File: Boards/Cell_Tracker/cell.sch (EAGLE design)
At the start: 26 parts, among them U2 LMR16020

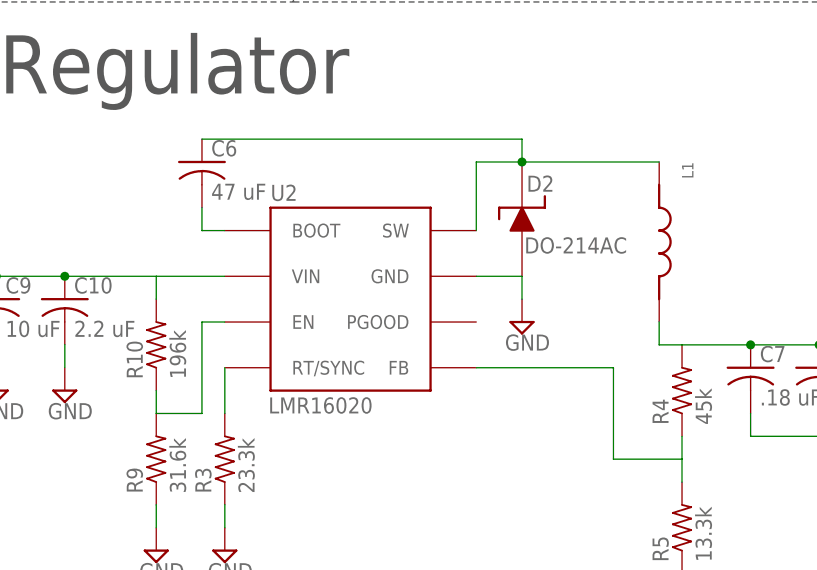
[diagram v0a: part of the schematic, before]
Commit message: Updated the inductor and mosfet in cell schematic
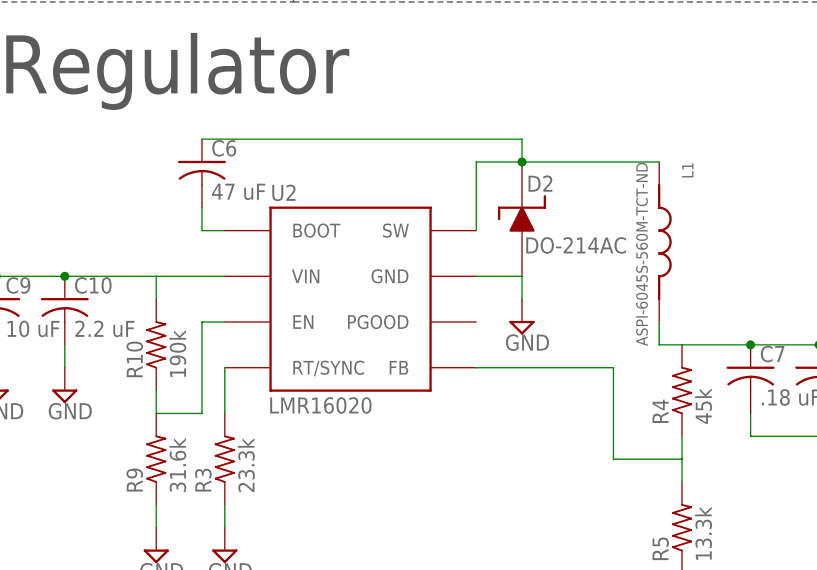
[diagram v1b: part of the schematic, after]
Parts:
- L1: value (none) -> ASPI-6045S-560M-TCT-ND; device inductors:587-2099-1-ND -> inductors:ASPI-6045S-560M-TCT-ND
- R10: value 196k -> 190k
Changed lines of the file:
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@@
 <?xml version="1.0" encoding="utf-8"?>
 <!DOCTYPE eagle SYSTEM "eagle.dtd">
-<eagle version="9.3.0">
+<eagle version="7.6.0">
 <drawing>
 <settings>
 <setting alwaysvectorfont="no"/>
-<setting keepoldvectorfont="yes"/>
 <setting verticaltext="up"/>
 </settings>
@@
 <part name="JP3" library="pinhead" deviceset="PINHD-1X2" device=""/>
 <part name="R9" library="resistor" deviceset="R-US_" device="R0603" value="31.6k"/>
-<part name="R10" library="resistor" deviceset="R-US_" device="R0603" value="196k"/>
+<part name="R10" library="resistor" deviceset="R-US_" device="R0603" value="190k"/>
 <part name="SUPPLY1" library="supply2" deviceset="GND" device=""/>
-<part name="L1" library="inductors" deviceset="587-2099-1-ND" device=""/>
+<part name="L1" library="inductors" deviceset="ASPI-6045S-560M-TCT-ND" device=""/>
 <part name="+3V6" library="supply1" deviceset="+3V3" device=""/>
 <part name="SUPPLY2" library="supply2" deviceset="GND" device=""/>

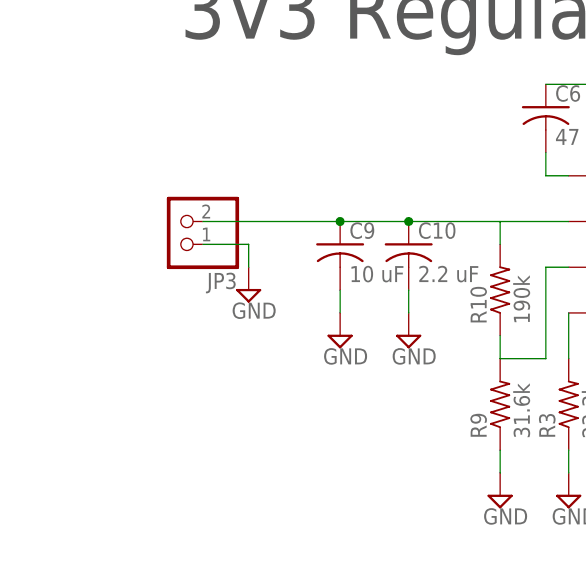
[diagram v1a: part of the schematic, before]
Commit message: put connector on cell board, plus lots of cad work
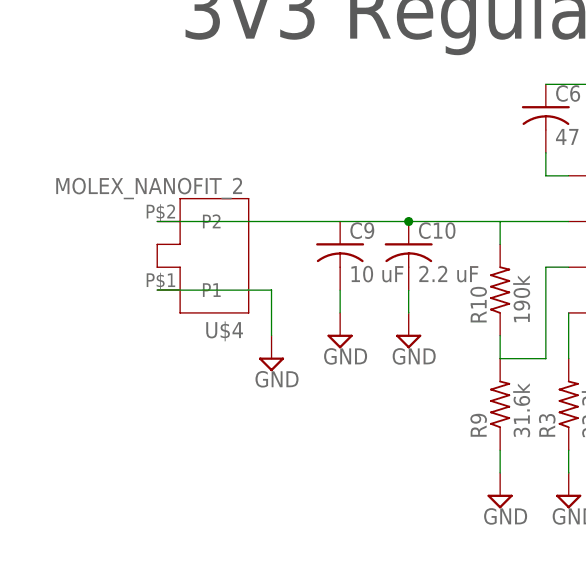
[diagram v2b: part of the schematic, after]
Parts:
- removed JP3: (no value), pinhead:PINHD-1X2
- added U$4: MOLEX_NANOFIT_2, cmdLibs:MOLEX_NANOFIT_2
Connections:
- net GND: now also U$4.P1; no longer JP3.1
- net VIN: now also U$4.P2; no longer JP3.2
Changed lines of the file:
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@@
 <part name="U2" library="HASP" deviceset="LMR16020" device=""/>
 <part name="D2" library="HASP" deviceset="DO-214AC" device=""/>
-<part name="JP3" library="pinhead" deviceset="PINHD-1X2" device=""/>
 <part name="R9" library="resistor" deviceset="R-US_" device="R0603" value="31.6k"/>
 <part name="R10" library="resistor" deviceset="R-US_" device="R0603" value="190k"/>
@@
 <part name="+3V7" library="supply1" deviceset="+3V3" device=""/>
 <part name="U$2" library="cmdLibs" deviceset="SI1013" device=""/>
+<part name="U$4" library="cmdLibs" deviceset="MOLEX_NANOFIT_2" device=""/>
 </parts>
 <sheets>
@@
 <attribute name="VALUE" x="86.614" y="91.44" size="1.778" layer="95"/>
 </instance>
-<instance part="JP3" gate="G$1" x="10.16" y="88.9" smashed="yes" rot="R180">
-<attribute name="NAME" x="16.51" y="83.185" size="1.778" layer="95" rot="R180"/>
-<attribute name="VALUE" x="16.51" y="93.98" size="1.778" layer="96" rot="R180"/>
-</instance>
 <instance part="R9" gate="G$1" x="45.72" y="68.58" smashed="yes" rot="R90">
 <attribute name="NAME" x="44.2214" y="64.77" size="1.778" layer="95" rot="R90"/>
@@
 <attribute name="VALUE" x="127" y="78.74" size="1.778" layer="96"/>
 </instance>
-<instance part="SUPPLY2" gate="GND" x="17.78" y="81.28" smashed="yes">
-<attribute name="VALUE" x="15.875" y="78.105" size="1.778" layer="96"/>
+<instance part="SUPPLY2" gate="GND" x="20.32" y="73.66" smashed="yes">
+<attribute name="VALUE" x="18.415" y="70.485" size="1.778" layer="96"/>
 </instance>
 <instance part="U$3" gate="G$1" x="208.28" y="172.72" smashed="yes"/>
@@
 <attribute name="NAME" x="209.042" y="132.08" size="1.778" layer="95" rot="R180"/>
 </instance>
+<instance part="U$4" gate="G$1" x="10.16" y="83.82" rot="R180"/>
 </instances>
 <busses>
@@
 </segment>
 <segment>
-<pinref part="JP3" gate="G$1" pin="1"/>
-<wire x1="12.7" y1="86.36" x2="17.78" y2="86.36" width="0.1524" layer="91"/>
-<wire x1="17.78" y1="86.36" x2="17.78" y2="83.82" width="0.1524" layer="91"/>
+<wire x1="20.32" y1="81.28" x2="20.32" y2="76.2" width="0.1524" layer="91"/>
 <pinref part="SUPPLY2" gate="GND" pin="GND"/>
+<pinref part="U$4" gate="G$1" pin="P1"/>
+<wire x1="7.62" y1="81.28" x2="20.32" y2="81.28" width="0.1524" layer="91"/>
 </segment>
 <segment>
@@
 <pinref part="C9" gate="G$1" pin="1"/>
 <pinref part="U2" gate="G$1" pin="VIN"/>
-<pinref part="JP3" gate="G$1" pin="2"/>
-<junction x="27.94" y="88.9"/>
-<wire x1="27.94" y1="88.9" x2="12.7" y2="88.9" width="0.1524" layer="91"/>
 <pinref part="R10" gate="G$1" pin="2"/>
 <wire x1="45.72" y1="86.36" x2="45.72" y2="88.9" width="0.1524" layer="91"/>
-</segment>
-</net>
+<pinref part="U$4" gate="G$1" pin="P2"/>
+<wire x1="7.62" y1="88.9" x2="27.94" y2="88.9" width="0.1524" layer="91"/>
+</segment>
+</net>

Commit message: All of the changes with CAD and electronics since switching to the microclasp connectors
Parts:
- added R7: (no value), resistor:R-US_R0603
- added U$5: (no value), NR_connectors:MICROCLASP
- U$4: value MOLEX_NANOFIT_2 -> (none); device cmdLibs:MOLEX_NANOFIT_2 -> NR_connectors:MICROCLASP
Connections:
- new net N$12: R7.1, U$5.P$1
- new net N$15: U$1.4/CAN-RX-PWM
- new net N$16: U$1.5/PWM
- new net N$33: U$1.6/PWM
- new net SWITCH_LED: R7.2, U$1.3/CAN-TX/PWM
- net GND: now also U$4.P$2, U$5.P$2; no longer U$4.P1
- net VIN: now also U$4.P$1; no longer U$4.P2
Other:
- note added: "LED Status"
- moved on the sheet: C10, C6, C7, C8, C9, COIN, D2, L1, R1, R10, R11, R2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

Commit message: fixes and design review slides
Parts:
- removed R7: (no value), resistor:R-US_R0603
- removed U$5: (no value), NR_connectors:MICROCLASP
- added R8: (no value), resistor:R-US_R0603
- R10: value 190k -> 195k
- R9: value 31.6k -> 39k
- U$4: value (none) -> MICROCLASP_4; device NR_connectors:MICROCLASP -> NR_connectors:MICROCLASP_4
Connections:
- removed net N$12: R7.1, U$5.P$1
- new net N$13: R8.2, U$4.P$2
- net GND: now also U$4.P$3, U$4.P$4; no longer U$4.P$2, U$5.P$2
- net SWITCH_LED: now also R8.1; no longer R7.2
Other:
- note removed: "LED Status"
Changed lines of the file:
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@@
 <part name="U2" library="HASP" deviceset="LMR16020" device=""/>
 <part name="D2" library="HASP" deviceset="DO-214AC" device=""/>
-<part name="R9" library="resistor" deviceset="R-US_" device="R0603" value="31.6k"/>
-<part name="R10" library="resistor" deviceset="R-US_" device="R0603" value="190k"/>
+<part name="R9" library="resistor" deviceset="R-US_" device="R0603" value="39k"/>
+<part name="R10" library="resistor" deviceset="R-US_" device="R0603" value="195k"/>
 <part name="SUPPLY1" library="supply1" deviceset="GND" device=""/>
 <part name="L1" library="inductors" deviceset="ASPI-6045S-560M-TCT-ND" device=""/>
 <part name="+3V6" library="supply1" deviceset="+3V3" device=""/>
-<part name="SUPPLY2" library="supply1" deviceset="GND" device=""/>
 <part name="U$3" library="NR_connectors" deviceset="MICRO_SD" device=""/>
 <part name="GND6" library="supply1" deviceset="GND" device=""/>
@@
 <part name="U$2" library="cmdLibs" deviceset="SI1013" device=""/>
 <part name="FRAME1" library="frames" deviceset="A4L-LOC" device=""/>
-<part name="U$4" library="NR_connectors" deviceset="MICROCLASP" device=""/>
-<part name="U$5" library="NR_connectors" deviceset="MICROCLASP" device=""/>
-<part name="GND1" library="supply1" deviceset="GND" device=""/>
-<part name="R7" library="resistor" deviceset="R-US_" device="R0603"/>
+<part name="U$4" library="NR_connectors" deviceset="MICROCLASP_4" device=""/>
+<part name="R8" library="resistor" deviceset="R-US_" device="R0603"/>
+<part name="SUPPLY2" library="supply1" deviceset="GND" device=""/>
 </parts>
 <sheets>
@@
 <wire x1="7.62" y1="88.9" x2="50.8" y2="88.9" width="0.1524" layer="97" style="longdash"/>
 <wire x1="50.8" y1="175.26" x2="50.8" y2="88.9" width="0.1524" layer="97" style="longdash"/>
-<text x="121.92" y="96.52" size="6.4516" layer="97">LED Status</text>
 <wire x1="144.78" y1="109.22" x2="144.78" y2="175.26" width="0.1524" layer="97" style="longdash"/>
 <wire x1="119.38" y1="88.9" x2="50.8" y2="88.9" width="0.1524" layer="97" style="longdash"/>
@@
 <wire x1="256.54" y1="109.22" x2="170.18" y2="109.22" width="0.1524" layer="97" style="longdash"/>
 <wire x1="170.18" y1="109.22" x2="144.78" y2="109.22" width="0.1524" layer="97" style="longdash"/>
-<wire x1="170.18" y1="109.22" x2="170.18" y2="71.12" width="0.1524" layer="97" style="longdash"/>
-<wire x1="170.18" y1="71.12" x2="119.38" y2="71.12" width="0.1524" layer="97" style="longdash"/>
 </plain>
 <instances>
@@
 <attribute name="VALUE" x="132.08" y="38.1" size="1.778" layer="96"/>
 </instance>
-<instance part="SUPPLY2" gate="1" x="25.4" y="33.02" smashed="yes">
-<attribute name="VALUE" x="23.495" y="29.845" size="1.778" layer="96"/>
-</instance>
 <instance part="U$3" gate="G$1" x="187.96" y="134.62" smashed="yes"/>
 <instance part="GND6" gate="1" x="208.28" y="124.46" smashed="yes">
@@
 </instance>
 <instance part="FRAME1" gate="G$1" x="0" y="0"/>
-<instance part="U$4" gate="G$1" x="10.16" y="48.26"/>
-<instance part="U$5" gate="G$1" x="127" y="86.36"/>
-<instance part="GND1" gate="1" x="139.7" y="78.74" smashed="yes">
-<attribute name="VALUE" x="137.16" y="76.2" size="1.778" layer="96"/>
-</instance>
-<instance part="R7" gate="G$1" x="144.78" y="86.36"/>
+<instance part="U$4" gate="G$1" x="7.62" y="43.18"/>
+<instance part="R8" gate="G$1" x="25.4" y="40.64" rot="R90"/>
+<instance part="SUPPLY2" gate="1" x="20.32" y="33.02" smashed="yes">
+<attribute name="VALUE" x="18.415" y="29.845" size="1.778" layer="96"/>
+</instance>
 </instances>
 <busses>
@@
 <wire x1="50.8" y1="22.86" x2="50.8" y2="20.32" width="0.1524" layer="91"/>
 <pinref part="SUPPLY1" gate="1" pin="GND"/>
-</segment>
-<segment>
-<pinref part="SUPPLY2" gate="1" pin="GND"/>
-<pinref part="U$4" gate="G$1" pin="P$2"/>
-<wire x1="25.4" y1="35.56" x2="25.4" y2="45.72" width="0.1524" layer="91"/>
-<wire x1="25.4" y1="45.72" x2="20.32" y2="45.72" width="0.1524" layer="91"/>
 </segment>
 <segment>
@@
 </segment>
 <segment>
-<pinref part="U$5" gate="G$1" pin="P$2"/>
-<wire x1="137.16" y1="83.82" x2="139.7" y2="83.82" width="0.1524" layer="91"/>
-<wire x1="139.7" y1="83.82" x2="139.7" y2="81.28" width="0.1524" layer="91"/>
-<pinref part="GND1" gate="1" pin="GND"/>
+<pinref part="U$4" gate="G$1" pin="P$3"/>
+<wire x1="17.78" y1="43.18" x2="20.32" y2="43.18" width="0.1524" layer="91"/>
+<wire x1="20.32" y1="43.18" x2="20.32" y2="40.64" width="0.1524" layer="91"/>
+<pinref part="U$4" gate="G$1" pin="P$4"/>
+<wire x1="20.32" y1="40.64" x2="20.32" y2="35.56" width="0.1524" layer="91"/>
+<wire x1="17.78" y1="40.64" x2="20.32" y2="40.64" width="0.1524" layer="91"/>
+<pinref part="SUPPLY2" gate="1" pin="GND"/>
 </segment>
 </net>
@@
 <pinref part="R10" gate="G$1" pin="2"/>
 <wire x1="50.8" y1="45.72" x2="50.8" y2="48.26" width="0.1524" layer="91"/>
-<wire x1="20.32" y1="48.26" x2="33.02" y2="48.26" width="0.1524" layer="91"/>
+<wire x1="17.78" y1="48.26" x2="33.02" y2="48.26" width="0.1524" layer="91"/>
 <pinref part="U$4" gate="G$1" pin="P$1"/>
 </segment>
@@
 </segment>
 </net>
-<net name="N$12" class="0">
-<segment>
-<pinref part="R7" gate="G$1" pin="1"/>
-<pinref part="U$5" gate="G$1" pin="P$1"/>
-<wire x1="139.7" y1="86.36" x2="137.16" y2="86.36" width="0.1524" layer="91"/>
-</segment>
-</net>
 <net name="SWITCH_LED" class="0">
 <segment>
@@
 </segment>
 <segment>
-<pinref part="R7" gate="G$1" pin="2"/>
-<wire x1="149.86" y1="86.36" x2="152.4" y2="86.36" width="0.1524" layer="91"/>
-<label x="152.4" y="86.36" size="1.016" layer="95" xref="yes"/>
+<pinref part="R8" gate="G$1" pin="1"/>
+<wire x1="25.4" y1="35.56" x2="25.4" y2="30.48" width="0.1524" layer="91"/>
+<label x="25.4" y="30.48" size="1.016" layer="95" xref="yes"/>
 </segment>
 </net>
@@
 </segment>
 </net>
+<net name="N$13" class="0">
+<segment>
+<pinref part="R8" gate="G$1" pin="2"/>
+<pinref part="U$4" gate="G$1" pin="P$2"/>
+<wire x1="25.4" y1="45.72" x2="17.78" y2="45.72" width="0.1524" layer="91"/>
+</segment>
+</net>

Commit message: Updated boards
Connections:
- removed net N$13: R8.2, U$4.P$2
- new net N$12: R8.2, U$4.P$1
- net VIN: now also U$4.P$2; no longer U$4.P$1
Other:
- moved on the sheet: R8, U$4
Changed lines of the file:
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@@
 <wire x1="119.38" y1="109.22" x2="119.38" y2="88.9" width="0.1524" layer="97" style="longdash"/>
 <wire x1="119.38" y1="109.22" x2="144.78" y2="109.22" width="0.1524" layer="97" style="longdash"/>
-<wire x1="119.38" y1="45.72" x2="119.38" y2="71.12" width="0.1524" layer="97" style="longdash"/>
-<wire x1="119.38" y1="71.12" x2="119.38" y2="88.9" width="0.1524" layer="97" style="longdash"/>
+<wire x1="119.38" y1="45.72" x2="119.38" y2="88.9" width="0.1524" layer="97" style="longdash"/>
 <wire x1="162.56" y1="45.72" x2="119.38" y2="45.72" width="0.1524" layer="97" style="longdash"/>
 <wire x1="162.56" y1="45.72" x2="162.56" y2="25.4" width="0.1524" layer="97" style="longdash"/>
-<wire x1="256.54" y1="109.22" x2="170.18" y2="109.22" width="0.1524" layer="97" style="longdash"/>
-<wire x1="170.18" y1="109.22" x2="144.78" y2="109.22" width="0.1524" layer="97" style="longdash"/>
+<wire x1="256.54" y1="109.22" x2="144.78" y2="109.22" width="0.1524" layer="97" style="longdash"/>
 </plain>
 <instances>
@@
 </instance>
 <instance part="FRAME1" gate="G$1" x="0" y="0"/>
-<instance part="U$4" gate="G$1" x="7.62" y="43.18"/>
-<instance part="R8" gate="G$1" x="25.4" y="40.64" rot="R90"/>
-<instance part="SUPPLY2" gate="1" x="20.32" y="33.02" smashed="yes">
-<attribute name="VALUE" x="18.415" y="29.845" size="1.778" layer="96"/>
+<instance part="U$4" gate="G$1" x="7.62" y="45.72"/>
+<instance part="R8" gate="G$1" x="22.86" y="55.88" rot="R180"/>
+<instance part="SUPPLY2" gate="1" x="20.32" y="35.56" smashed="yes">
+<attribute name="VALUE" x="18.415" y="32.385" size="1.778" layer="96"/>
 </instance>
 </instances>
@@
 <segment>
 <pinref part="U$4" gate="G$1" pin="P$3"/>
+<wire x1="17.78" y1="45.72" x2="20.32" y2="45.72" width="0.1524" layer="91"/>
+<wire x1="20.32" y1="45.72" x2="20.32" y2="43.18" width="0.1524" layer="91"/>
+<pinref part="U$4" gate="G$1" pin="P$4"/>
+<wire x1="20.32" y1="43.18" x2="20.32" y2="38.1" width="0.1524" layer="91"/>
 <wire x1="17.78" y1="43.18" x2="20.32" y2="43.18" width="0.1524" layer="91"/>
-<wire x1="20.32" y1="43.18" x2="20.32" y2="40.64" width="0.1524" layer="91"/>
-<pinref part="U$4" gate="G$1" pin="P$4"/>
-<wire x1="20.32" y1="40.64" x2="20.32" y2="35.56" width="0.1524" layer="91"/>
-<wire x1="17.78" y1="40.64" x2="20.32" y2="40.64" width="0.1524" layer="91"/>
 <pinref part="SUPPLY2" gate="1" pin="GND"/>
 </segment>
@@
 <pinref part="R10" gate="G$1" pin="2"/>
 <wire x1="50.8" y1="45.72" x2="50.8" y2="48.26" width="0.1524" layer="91"/>
+<pinref part="U$4" gate="G$1" pin="P$2"/>
 <wire x1="17.78" y1="48.26" x2="33.02" y2="48.26" width="0.1524" layer="91"/>
-<pinref part="U$4" gate="G$1" pin="P$1"/>
 </segment>
 </net>
@@
 <segment>
 <pinref part="R8" gate="G$1" pin="1"/>
-<wire x1="25.4" y1="35.56" x2="25.4" y2="30.48" width="0.1524" layer="91"/>
-<label x="25.4" y="30.48" size="1.016" layer="95" xref="yes"/>
+<wire x1="27.94" y1="55.88" x2="33.02" y2="55.88" width="0.1524" layer="91"/>
+<label x="33.02" y="55.88" size="1.016" layer="95" xref="yes"/>
 </segment>
 </net>
@@
 </segment>
 </net>
-<net name="N$13" class="0">
+<net name="N$12" class="0">
 <segment>
 <pinref part="R8" gate="G$1" pin="2"/>
-<pinref part="U$4" gate="G$1" pin="P$2"/>
-<wire x1="25.4" y1="45.72" x2="17.78" y2="45.72" width="0.1524" layer="91"/>
-</segment>
-</net>
+<pinref part="U$4" gate="G$1" pin="P$1"/>
+<wire x1="17.78" y1="55.88" x2="17.78" y2="50.8" width="0.1524" layer="91"/>
+</segment>
+</net>
